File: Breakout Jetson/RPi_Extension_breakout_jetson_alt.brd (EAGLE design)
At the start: 63 x 70.1 mm, 24 parts, among them U1 Value, U10 74AHC1G04GW/T1, U11 74AHC1G04GW/T1, U12 74AHC1G04GW/T1, U13 74AHC1G04GW/T1, U14 74AHC1G04GW/T1, U15 74AHC1G04GW/T1, U16 74AHC1G04GW/T1, U17 74AHC1G04GW/T1, U2 74AHC1G04GW/T1, U3 74AHC1G04GW/T1, U4 74AHC1G04GW/T1, U5 74AHC1G04GW/T1, U6 74AHC1G04GW/T1, U7 74AHC1G04GW/T1, U8 74AHC1G04GW/T1, U9 74AHC1G04GW/T1

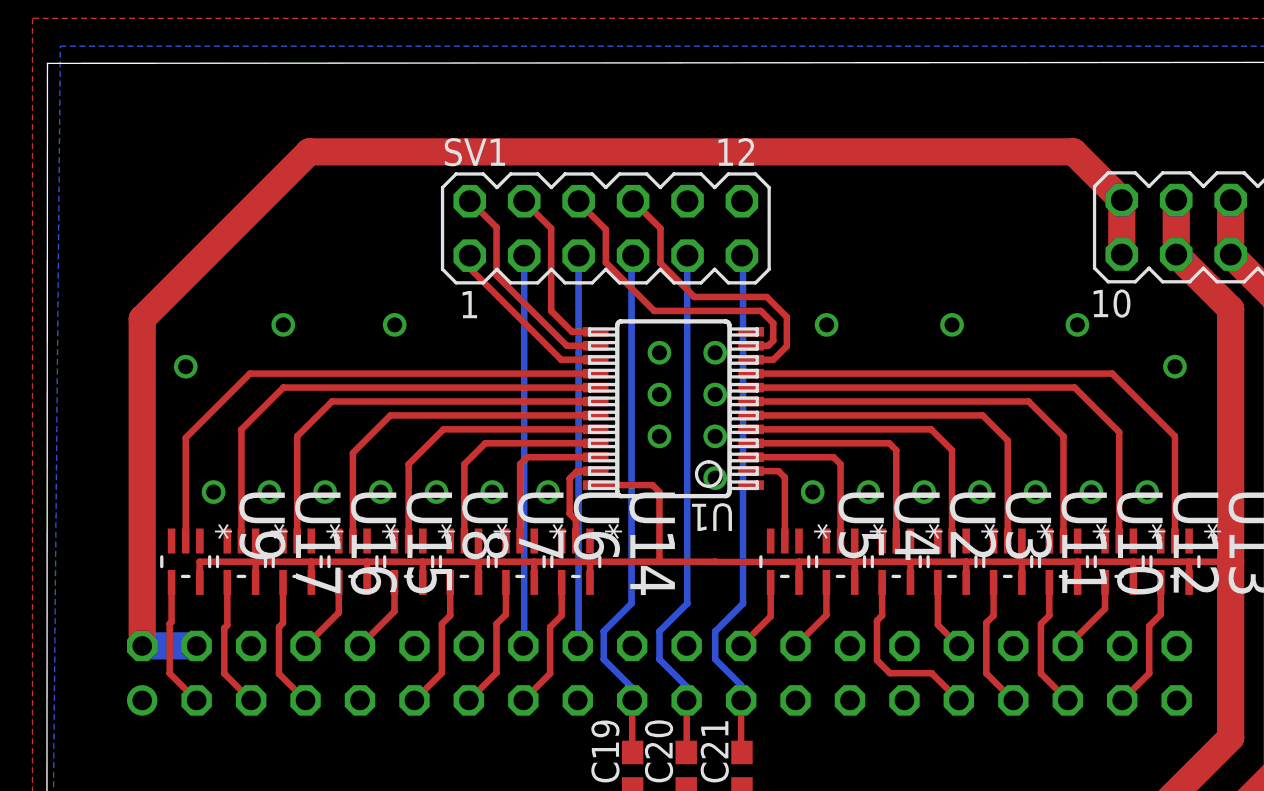
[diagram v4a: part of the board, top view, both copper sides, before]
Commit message: rearranged pins on jetson board for a nicer layout
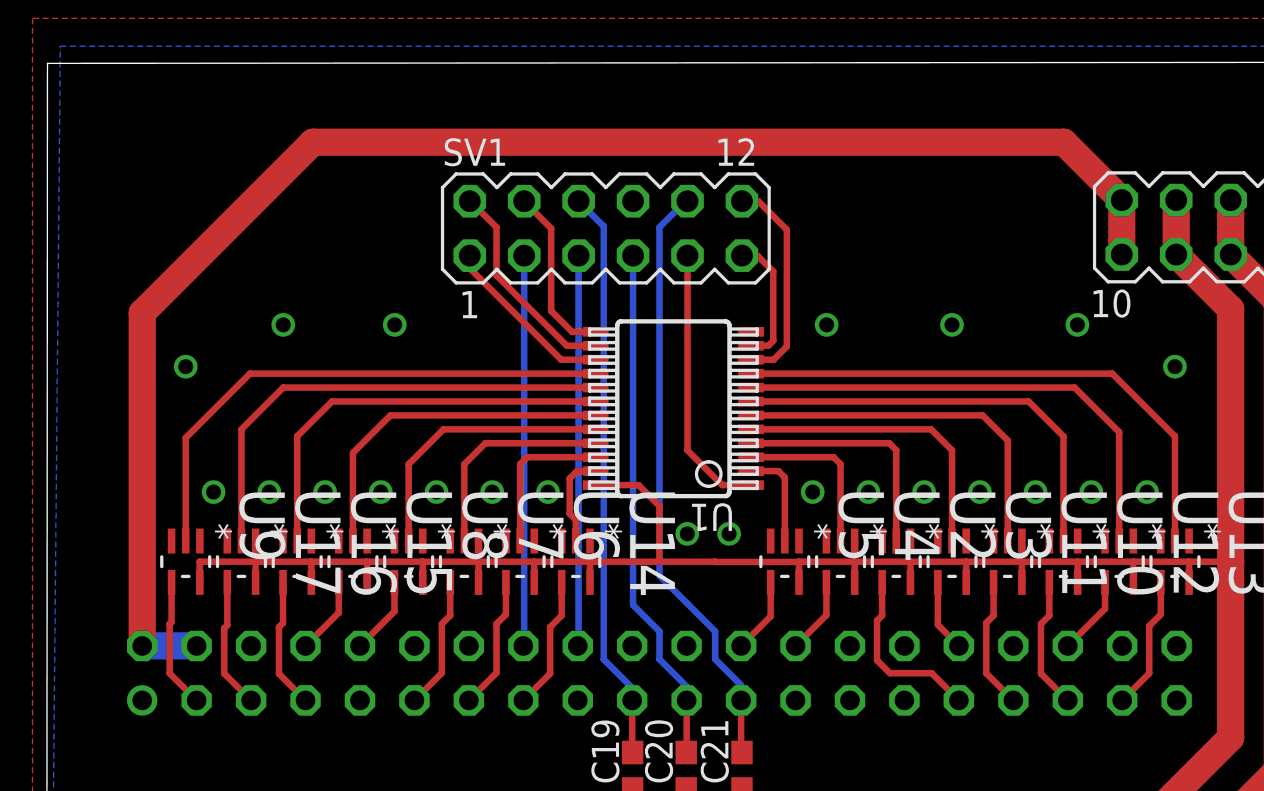
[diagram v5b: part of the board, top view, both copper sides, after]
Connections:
- removed net ADDR4: SV1.10
- removed net ADDR5: SV1.12
- new net IO_SIGNAL: SV1.9, U1.1
- net ADDR2: now also SV1.11; no longer SV1.6
- net ADDR3: now also SV1.12; no longer SV1.8
- net GND: now also SV1.8
- net MISO: now also SV1.7; no longer SV1.9
- net MOSI: now also SV1.6; no longer SV1.7
- net SCLK: now also SV1.10; no longer SV1.11
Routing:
- net IO_SIGNAL: track 0.00 -> 12.7 mm
- net ADDR2: track 14.3 -> 6.13 mm
- net SCLK: track 24.3 -> 27.9 mm
- net ADDR3: track 13.7 -> 10.0 mm
- net MOSI: track 24.3 -> 26.8 mm
- net +5V: track 70.2 -> 70.7 mm
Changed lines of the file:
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@@
 <via x="51.35" y="50.05" extent="1-16" drill="0.7"/>
 <via x="23.4" y="50.05" extent="1-16" drill="0.7"/>
-<via x="28.6" y="52.65" extent="1-16" drill="0.7"/>
-<via x="28.6" y="54.6" extent="1-16" drill="0.7"/>
-<via x="28.6" y="56.55" extent="1-16" drill="0.7"/>
-<via x="31.2" y="50.7" extent="1-16" drill="0.7"/>
 <via x="6.5" y="55.9" extent="1-16" drill="0.7"/>
 <via x="52.65" y="55.9" extent="1-16" drill="0.7"/>
@@
 <via x="11.05" y="57.85" extent="1-16" drill="0.7"/>
 <via x="48.1" y="57.85" extent="1-16" drill="0.7"/>
-<via x="31.2" y="56.55" extent="1-16" drill="0.7"/>
-<via x="31.2" y="54.6" extent="1-16" drill="0.7"/>
-<via x="31.2" y="52.65" extent="1-16" drill="0.7"/>
 <contactref element="U1" pad="12"/>
+<contactref element="SV1" pad="8"/>
+<via x="29.9" y="48.1" extent="1-16" drill="0.7"/>
+<via x="31.85" y="48.1" extent="1-16" drill="0.7"/>
 </signal>
 <signal name="DVCC">
@@
 <via x="3.25" y="24.05" extent="1-16" drill="0.7"/>
 <via x="3.28" y="24.05" extent="1-16" drill="0.7"/>
-<wire x1="25.624996875" y1="50.375" x2="28.275" y2="50.375" width="0.3048" layer="1"/>
 <contactref element="U5" pad="5"/>
 <contactref element="U4" pad="5"/>
@@
 <wire x1="7.15" y1="46.8" x2="9.75" y2="46.8" width="0.3048" layer="1"/>
 <wire x1="35.1104" y1="46.7896" x2="31.2104" y2="46.7896" width="0.3048" layer="1"/>
-<wire x1="28.275" y1="50.375" x2="28.6" y2="50.05" width="0.3048" layer="1"/>
-<wire x1="28.6" y1="50.05" x2="28.6" y2="46.8" width="0.3048" layer="1"/>
-<wire x1="28.6" y1="46.8" x2="31.2" y2="46.8" width="0.3048" layer="1"/>
 <wire x1="31.2" y1="46.8" x2="31.2104" y2="46.7896" width="0.3048" layer="1"/>
 <wire x1="25.35" y1="46.8" x2="28.6" y2="46.8" width="0.3048" layer="1"/>
+<wire x1="28.6" y1="46.8" x2="31.2" y2="46.8" width="0.3048" layer="1"/>
 <wire x1="53.3104" y1="45.8348" x2="53.3104" y2="46.7896" width="0.3048" layer="1"/>
 <wire x1="53.3104" y1="46.7896" x2="53.3" y2="46.8" width="0.3048" layer="1"/>
 <wire x1="53.3" y1="46.8" x2="55.25" y2="46.8" width="0.3048" layer="1"/>
+<wire x1="25.624996875" y1="50.375" x2="27.625" y2="50.375" width="0.3048" layer="1"/>
+<wire x1="27.625" y1="50.375" x2="28.6" y2="49.4" width="0.3048" layer="1"/>
+<wire x1="28.6" y1="49.4" x2="28.6" y2="46.8" width="0.3048" layer="1"/>
 </signal>
 <signal name="MISO">
@@
 <wire x1="29.87" y1="40.33" x2="29.87" y2="37.92" width="0.3048" layer="1"/>
 <wire x1="29.87" y1="37.92" x2="29.85" y2="37.9" width="0.4064" layer="1"/>
-<contactref element="SV1" pad="9"/>
 <wire x1="29.87" y1="40.33" x2="29.87" y2="40.98" width="0.3048" layer="16"/>
 <wire x1="29.87" y1="40.98" x2="28.6" y2="42.25" width="0.3048" layer="16"/>
 <wire x1="28.6" y1="42.25" x2="28.6" y2="43.55" width="0.3048" layer="16"/>
-<wire x1="28.6" y1="43.55" x2="29.9" y2="44.85" width="0.3048" layer="16"/>
-<wire x1="29.9" y1="44.85" x2="29.9" y2="61.07" width="0.3048" layer="16"/>
-<wire x1="29.9" y1="61.07" x2="29.91" y2="61.08" width="0.3048" layer="16"/>
+<contactref element="SV1" pad="7"/>
+<wire x1="27.37" y1="61.08" x2="27.37" y2="44.78" width="0.3048" layer="16"/>
+<wire x1="27.37" y1="44.78" x2="28.6" y2="43.55" width="0.3048" layer="16"/>
 </signal>
 <signal name="SCLK">
@@
 <wire x1="32.41" y1="40.33" x2="32.41" y2="37.94" width="0.3048" layer="1"/>
 <wire x1="32.41" y1="37.94" x2="32.45" y2="37.9" width="0.4064" layer="1"/>
-<contactref element="SV1" pad="11"/>
 <wire x1="32.41" y1="40.33" x2="32.41" y2="41.04" width="0.3048" layer="16"/>
 <wire x1="32.41" y1="41.04" x2="31.2" y2="42.25" width="0.3048" layer="16"/>
 <wire x1="31.2" y1="42.25" x2="31.2" y2="43.55" width="0.3048" layer="16"/>
-<wire x1="31.2" y1="43.55" x2="32.5" y2="44.85" width="0.3048" layer="16"/>
-<wire x1="32.5" y1="44.85" x2="32.5" y2="61.03" width="0.3048" layer="16"/>
-<wire x1="32.5" y1="61.03" x2="32.45" y2="61.08" width="0.3048" layer="16"/>
+<contactref element="SV1" pad="10"/>
+<wire x1="29.91" y1="63.62" x2="29.82" y2="63.62" width="0.3048" layer="16"/>
+<wire x1="29.82" y1="63.62" x2="28.6" y2="62.4" width="0.3048" layer="16"/>
+<wire x1="28.6" y1="62.4" x2="28.6" y2="46.15" width="0.3048" layer="16"/>
+<wire x1="28.6" y1="46.15" x2="29.9" y2="44.85" width="0.3048" layer="16"/>
+<wire x1="29.9" y1="44.85" x2="31.2" y2="43.55" width="0.3048" layer="16"/>
 </signal>
 <signal name="VDD">
@@
 <wire x1="27.33" y1="40.33" x2="27.33" y2="37.92" width="0.3048" layer="1"/>
 <wire x1="27.33" y1="37.92" x2="27.35" y2="37.9" width="0.4064" layer="1"/>
-<contactref element="SV1" pad="7"/>
 <wire x1="27.33" y1="40.33" x2="27.33" y2="40.92" width="0.3048" layer="16"/>
 <wire x1="27.33" y1="40.92" x2="26" y2="42.25" width="0.3048" layer="16"/>
-<wire x1="26" y1="42.25" x2="26" y2="43.55" width="0.3048" layer="16"/>
-<wire x1="26" y1="43.55" x2="27.3" y2="44.85" width="0.3048" layer="16"/>
-<wire x1="27.3" y1="44.85" x2="27.3" y2="61.01" width="0.3048" layer="16"/>
-<wire x1="27.3" y1="61.01" x2="27.37" y2="61.08" width="0.3048" layer="16"/>
+<contactref element="SV1" pad="6"/>
+<wire x1="26" y1="42.25" x2="26" y2="62.45" width="0.3048" layer="16"/>
+<wire x1="26" y1="62.45" x2="24.83" y2="63.62" width="0.3048" layer="16"/>
 </signal>
 <signal name="+5V">
@@
 <contactref element="SV2" pad="9"/>
 <wire x1="50.17" y1="63.67" x2="50.17" y2="61.13" width="1.27" layer="1"/>
-<wire x1="50.17" y1="63.67" x2="47.918590625" y2="65.921409375" width="1.27" layer="1"/>
-<wire x1="47.918590625" y1="65.921409375" x2="12.26083125" y2="65.921409375" width="1.27" layer="1"/>
-<wire x1="12.26083125" y1="65.921409375" x2="4.47" y2="58.130578125" width="1.27" layer="1"/>
-<wire x1="4.47" y1="58.130578125" x2="4.47" y2="42.87" width="1.27" layer="1"/>
+<wire x1="50.17" y1="63.67" x2="47.4687625" y2="66.3712375" width="1.27" layer="1"/>
+<wire x1="47.4687625" y1="66.3712375" x2="12.431075" y2="66.3712375" width="1.27" layer="1"/>
+<wire x1="12.431075" y1="66.3712375" x2="4.47" y2="58.4101625" width="1.27" layer="1"/>
+<wire x1="4.47" y1="58.4101625" x2="4.47" y2="42.87" width="1.27" layer="1"/>
 <wire x1="4.47" y1="42.87" x2="7.01" y2="42.87" width="1.27" layer="16"/>
 </signal>
@@
 </signal>
 <signal name="ADDR2">
-<contactref element="SV1" pad="6"/>
 <contactref element="U1" pad="11"/>
-<wire x1="24.83" y1="63.62" x2="24.83" y2="63.57" width="0.3048" layer="1"/>
-<wire x1="24.83" y1="63.57" x2="26.1" y2="62.3" width="0.3048" layer="1"/>
-<wire x1="26.1" y1="62.3" x2="26.1" y2="60.75886875" width="0.3048" layer="1"/>
-<wire x1="26.1" y1="60.75886875" x2="28.35886875" y2="58.5" width="0.3048" layer="1"/>
 <wire x1="32.875" y1="56.875" x2="33.67793125" y2="56.875" width="0.3048" layer="1"/>
 <wire x1="33.67793125" y1="56.875" x2="33.91106875" y2="57.1081375" width="0.3048" layer="1"/>
-<wire x1="33.91106875" y1="57.1081375" x2="33.91106875" y2="57.92795625" width="0.3048" layer="1"/>
-<wire x1="33.91106875" y1="57.92795625" x2="33.339025" y2="58.5" width="0.3048" layer="1"/>
-<wire x1="33.339025" y1="58.5" x2="28.35886875" y2="58.5" width="0.3048" layer="1"/>
+<contactref element="SV1" pad="11"/>
+<wire x1="33.91106875" y1="57.1081375" x2="33.91106875" y2="60.33893125" width="0.3048" layer="1"/>
+<wire x1="32.45" y1="61.08" x2="33.17" y2="61.08" width="0.3048" layer="1"/>
+<wire x1="33.17" y1="61.08" x2="33.91106875" y2="60.33893125" width="0.3048" layer="1"/>
 </signal>
 <signal name="EN_MULT">
@@
 </signal>
 <signal name="ADDR3">
-<contactref element="SV1" pad="8"/>
 <contactref element="U1" pad="10"/>
-<wire x1="27.37" y1="63.62" x2="27.38" y2="63.62" width="0.3048" layer="1"/>
-<wire x1="27.38" y1="63.62" x2="28.65" y2="62.35" width="0.3048" layer="1"/>
-<wire x1="32.875" y1="56.225003125" x2="33.916221875" y2="56.225003125" width="0.3048" layer="1"/>
-<wire x1="33.916221875" y1="56.225003125" x2="34.5437375" y2="56.85251875" width="0.3048" layer="1"/>
-<wire x1="34.5437375" y1="56.85251875" x2="34.5437375" y2="58.2181125" width="0.3048" layer="1"/>
-<wire x1="34.5437375" y1="58.2181125" x2="33.61185" y2="59.15" width="0.3048" layer="1"/>
-<wire x1="33.61185" y1="59.15" x2="30.2311375" y2="59.15" width="0.3048" layer="1"/>
-<wire x1="30.2311375" y1="59.15" x2="28.65" y2="60.7311375" width="0.3048" layer="1"/>
-<wire x1="28.65" y1="60.7311375" x2="28.65" y2="62.35" width="0.3048" layer="1"/>
-</signal>
-<signal name="ADDR4">
-<contactref element="SV1" pad="10"/>
-</signal>
-<signal name="ADDR5">
+<wire x1="32.875" y1="56.225003125" x2="33.929309375" y2="56.225003125" width="0.3048" layer="1"/>
+<wire x1="33.929309375" y1="56.225003125" x2="34.5437375" y2="56.83943125" width="0.3048" layer="1"/>
+<wire x1="34.5437375" y1="56.83943125" x2="34.5437375" y2="62.287740625" width="0.3048" layer="1"/>
 <contactref element="SV1" pad="12"/>
+<wire x1="34.5437375" y1="62.287740625" x2="33.211478125" y2="63.62" width="0.3048" layer="1"/>
+<wire x1="33.211478125" y1="63.62" x2="32.45" y2="63.62" width="0.3048" layer="1"/>
 </signal>
 <signal name="LDAC">
@@
 <wire x1="8.3" y1="41.58" x2="9.55" y2="40.33" width="0.3048" layer="1"/>
 </signal>
+<signal name="IO_SIGNAL">
+<contactref element="U1" pad="1"/>
+<wire x1="32.875" y1="50.375" x2="31.525" y2="50.375" width="0.3048" layer="1"/>
+<contactref element="SV1" pad="9"/>
+<wire x1="29.91" y1="61.08" x2="29.91" y2="51.99" width="0.3048" layer="1"/>
+<wire x1="29.91" y1="51.99" x2="31.525" y2="50.375" width="0.3048" layer="1"/>
+</signal>
 </signals>

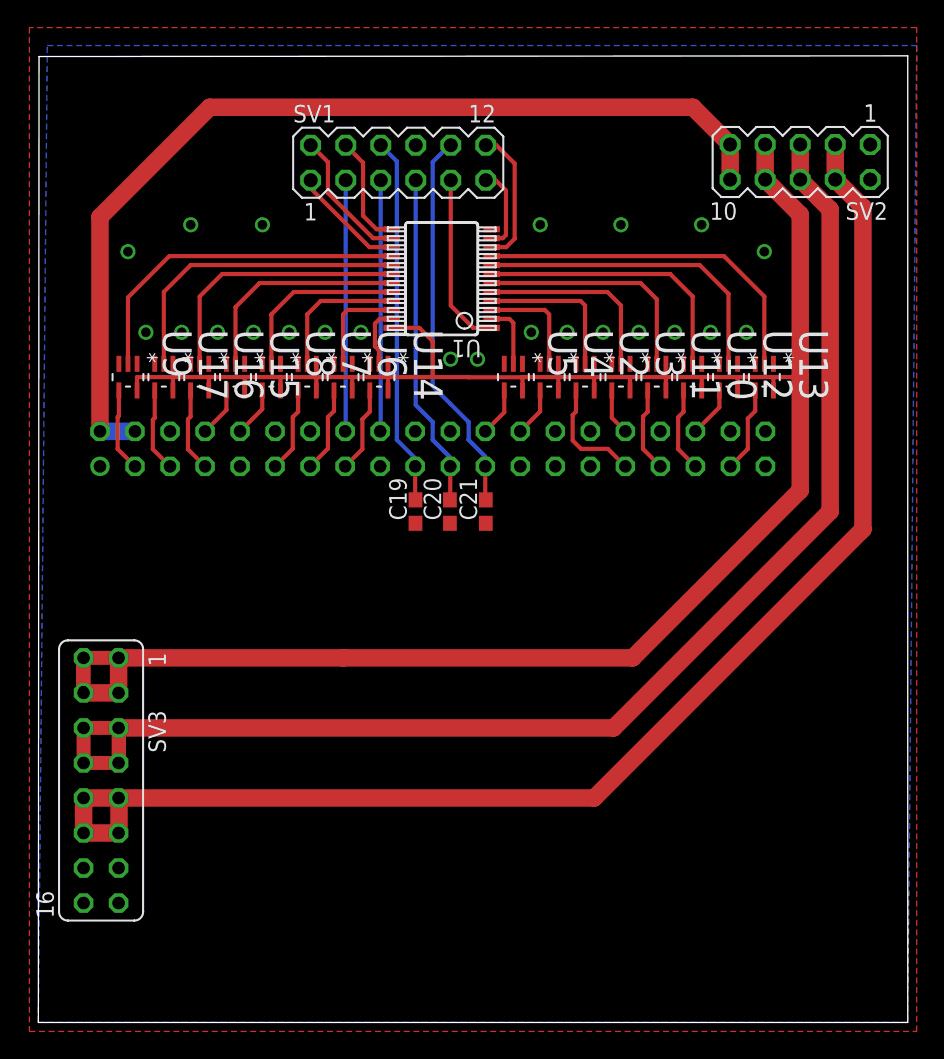
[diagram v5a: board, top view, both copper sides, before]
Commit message: fixed drc errors on jetson tx1 board
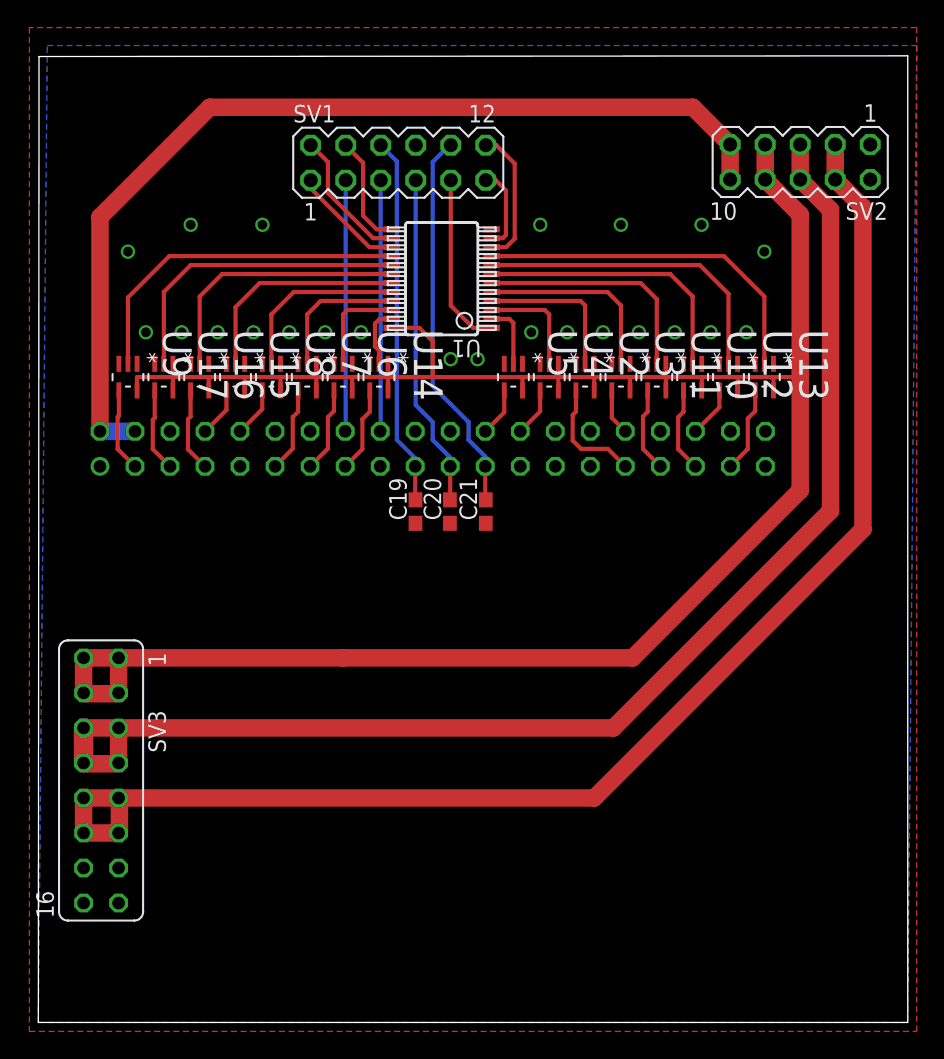
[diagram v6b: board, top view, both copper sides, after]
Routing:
- net VDD: track 98.3 -> 95.8 mm, vias 3 -> 0
- net DVCC: track 169.2 -> 166.9 mm, vias 2 -> 0
- net VSS: track 101.0 -> 100.9 mm, vias 1 -> 0
